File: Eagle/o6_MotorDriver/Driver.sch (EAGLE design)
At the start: 17 parts, among them IC1 ULN2003AD, IC2 REG1117, P1C2 10uF, P1C3 10uF

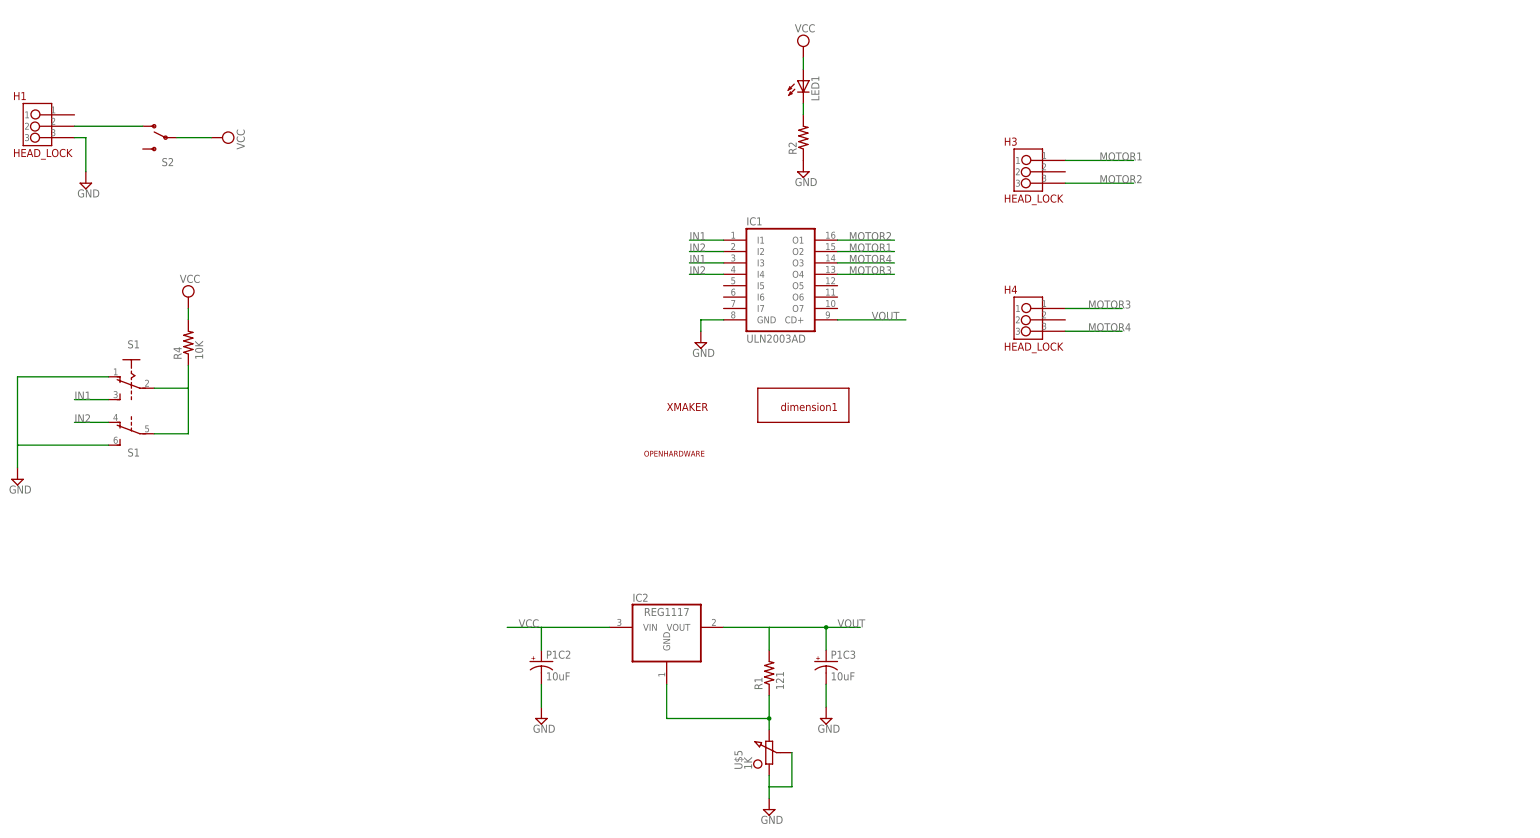
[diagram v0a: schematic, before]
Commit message: change motordriver
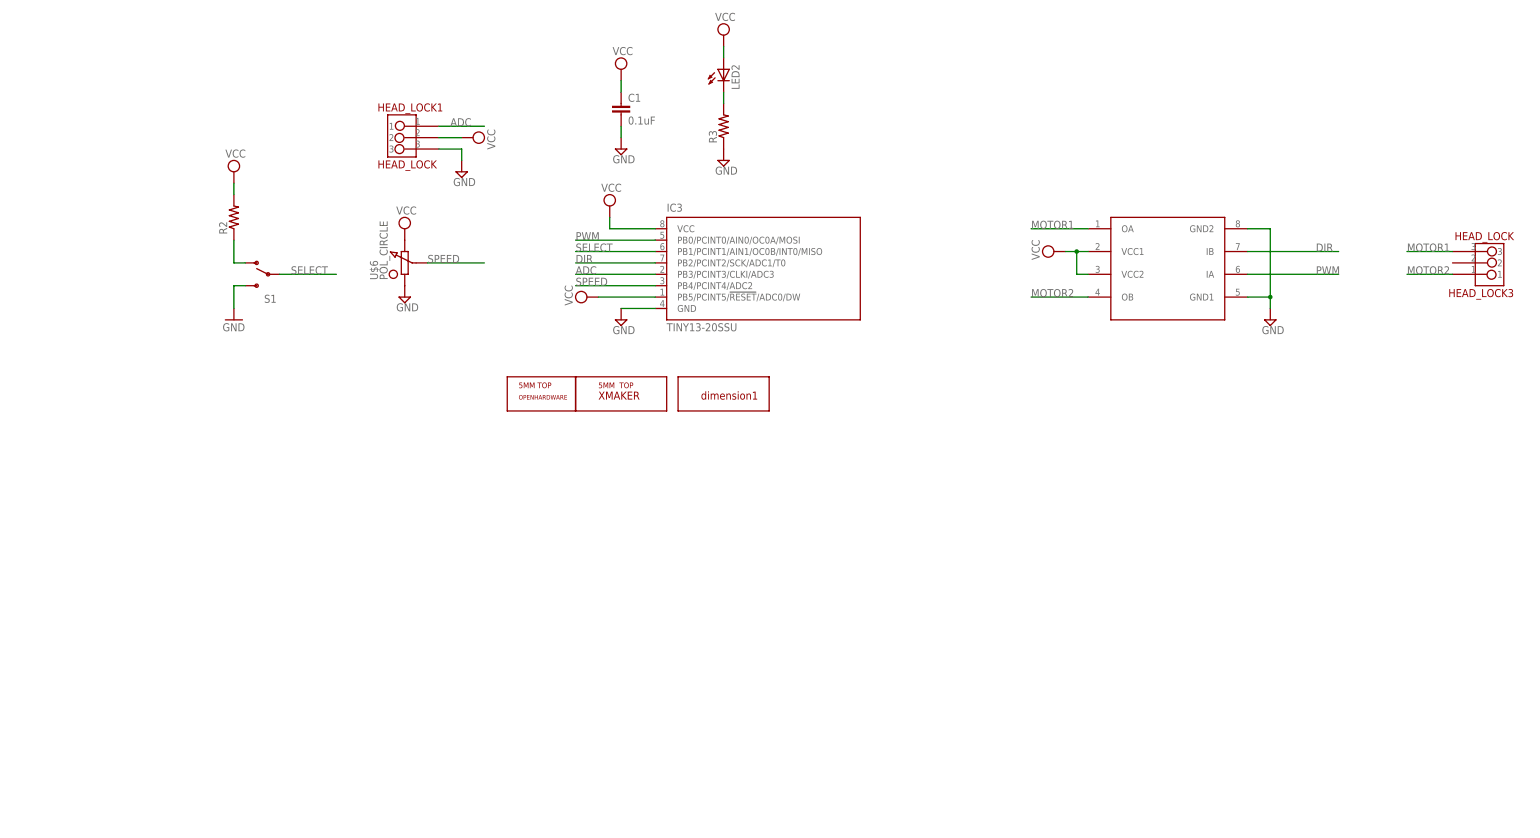
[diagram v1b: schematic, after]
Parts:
- removed H1, H3, H4: HEAD_LOCK, HEAD_LOCK:HEAD_LOCK
- removed IC1: ULN2003AD, uln-udn:ULN2003AD
- removed IC2: REG1117, burr-brown:REG1117
- removed LED1: (no value), eagle-ltspice:LED_ESML0603
- removed P1C2, P1C3: 10uF, SparkFun:CAP_POL1206
- removed R1: 121, SparkFun-Resistors:0.27OHM-1/10W-1%(0603)
- removed R4: 10K, SparkFun-Resistors:0.27OHM-1/10W-1%(0603)
- removed S2: (no value), SparkFun-Electromechanical:SWITCH-SPDTKIT
- removed U$3: DIMENSION1, Xmaker_yuhui:DIMENSION1
- removed U$4: OPENHARDWARE, Xmaker_yuhui:OPENHARDWARE
- removed U$5: 1K, Xmaker_yuhui:POL_CIRCLE
- added C1: 0.1uF, SparkFun-Passives:CAP0603-CAP
- added HEAD_LOCK1, HEAD_LOCK3: HEAD_LOCK, Xmaker_yuhui:HEAD_LOCK
- added IC3: TINY13-20SSU, atmel:TINY13-20SSU
- added LED2: (no value), eagle-ltspice:LED_ESML0603
- added R3: (no value), SparkFun-Resistors:0.27OHM-1/10W-1%(0603)
- added U$1: DIMENSION1, Xmaker_yuhui:DIMENSION1
- added U$6: POL_CIRCLE, Xmaker_yuhui:POL_CIRCLE
- added U$7: XMAKERLOGO_5MM_TOP, Xmaker_yuhui:XMAKERLOGO_5MM_TOP
- added U$8: OPENHARDWARE_5MM_TOP, Xmaker_yuhui:OPENHARDWARE_5MM_TOP
- R2: device SparkFun-Resistors:0.27OHM-1/10W-1%(0603) -> SparkFun-Passives:RESISTOR0603-RES
- S1: device switch:A68-A31 -> SparkFun-Electromechanical:SWITCH-SPDTKIT
- U$2: value XMAKERLOGO2 -> L9110; device Xmaker_yuhui:XMAKERLOGO2 -> Xmaker_yuhui:L9110
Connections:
- removed net IN1: IC1.I1, IC1.I3, S1A.S
- removed net IN2: IC1.I2, IC1.I4, S1B.O
- removed net MOTOR3: H4.1, IC1.O4
- removed net MOTOR4: H4.3, IC1.O3
- removed net N$1: LED1.C, R2.2
- removed net N$3: IC2.GND, R1.1, U$5.1
- removed net N$4: H1.2, S2.O
- removed net VOUT: IC1.CD+, IC2.VOUT, P1C3.+, R1.2
- new net ADC: HEAD_LOCK1.1, IC3.PB3/PCINT3/CLKI/ADC3
- new net DIR: IC3.PB2/PCINT2/SCK/ADC1/T0, U$2.IB
- new net N$5: LED2.C, R3.2
- new net PWM: IC3.PB0/PCINT0/AIN0/OC0A/MOSI, U$2.IA
- new net SELECT: IC3.PB1/PCINT1/AIN1/OC0B/INT0/MISO, S1.P
- new net SPEED: IC3.PB4/PCINT4/ADC2, U$6.2
- net GND: now also C1.2, HEAD_LOCK1.3, IC3.GND, R3.1, S1.S, U$2.GND1, U$2.GND2, U$6.3; no longer H1.3, IC1.GND, P1C2.-, P1C3.-, R2.1, S1A.O, S1B.S, U$5.2, U$5.3
- net MOTOR1: now also HEAD_LOCK3.3, U$2.OA; no longer H3.1, IC1.O2
- net MOTOR2: now also HEAD_LOCK3.1, U$2.OB; no longer H3.3, IC1.O1
- net N$2: now also R2.1, S1.O; no longer R4.1, S1A.P, S1B.P
- net VCC: now also C1.1, HEAD_LOCK1.2, IC3.PB5/PCINT5/!RESET!/ADC0/DW, IC3.VCC, LED2.A, R2.2, U$2.VCC1, U$2.VCC2, U$6.1; no longer IC2.VIN, LED1.A, P1C2.+, R4.2, S2.P
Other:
- moved on the sheet: R2

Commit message: 12.15
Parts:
- removed HEAD_LOCK1, HEAD_LOCK3: HEAD_LOCK, Xmaker_yuhui:HEAD_LOCK
- added HEAD_LOCK2: HEAD_LOCK, Xmaker:HEAD_LOCK
- added U$4: HEAD_LOCK2, Xmaker:HEAD_LOCK2
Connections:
- net ADC: now also HEAD_LOCK2.1; no longer HEAD_LOCK1.1
- net GND: now also HEAD_LOCK2.3; no longer HEAD_LOCK1.3
- net MOTOR1: now also U$4.2; no longer HEAD_LOCK3.3
- net MOTOR2: now also U$4.1; no longer HEAD_LOCK3.1
- net VCC: now also HEAD_LOCK2.2; no longer HEAD_LOCK1.2
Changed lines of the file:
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@@
 <?xml version="1.0" encoding="utf-8"?>
 <!DOCTYPE eagle SYSTEM "eagle.dtd">
-<eagle version="7.2.0">
+<eagle version="6.6.0">
 <drawing>
 <settings>
@@
 <setting verticaltext="up"/>
 </settings>
-<grid distance="0.1" unitdist="inch" unit="inch" style="lines" multiple="1" display="no" altdistance="0.01" altunitdist="inch" altunit="inch"/>
+<grid distance="10" unitdist="mil" unit="mil" style="lines" multiple="1" display="no" altdistance="0.01" altunitdist="inch" altunit="inch"/>
 <layers>
 <layer number="1" name="Top" color="4" fill="1" visible="no" active="no"/>
@@
 <part name="U$1" library="Xmaker_yuhui" deviceset="DIMENSION1" device=""/>
 <part name="U$6" library="Xmaker_yuhui" deviceset="POL_CIRCLE" device=""/>
-<part name="HEAD_LOCK1" library="Xmaker_yuhui" deviceset="HEAD_LOCK" device=""/>
 <part name="U$7" library="Xmaker_yuhui" deviceset="XMAKERLOGO_5MM_TOP" device=""/>
 <part name="U$8" library="Xmaker_yuhui" deviceset="OPENHARDWARE_5MM_TOP" device=""/>
@@
 <part name="SUPPLY1" library="supply2" deviceset="VCC" device=""/>
 <part name="SUPPLY3" library="supply2" deviceset="GND" device=""/>
-<part name="HEAD_LOCK3" library="Xmaker_yuhui" deviceset="HEAD_LOCK" device=""/>
 <part name="SUPPLY2" library="supply2" deviceset="VCC" device=""/>
+<part name="HEAD_LOCK2" library="Xmaker" deviceset="HEAD_LOCK" device=""/>
+<part name="U$4" library="Xmaker" deviceset="HEAD_LOCK2" device=""/>
 </parts>
 <sheets>
@@
 <instance part="U$1" gate="G$1" x="-5.08" y="-25.4"/>
 <instance part="U$6" gate="G$1" x="-76.2" y="5.08"/>
-<instance part="HEAD_LOCK1" gate="G$1" x="-76.2" y="33.02"/>
 <instance part="U$7" gate="G$1" x="-27.94" y="-22.86"/>
 <instance part="U$8" gate="G$1" x="-45.72" y="-25.4"/>
@@
 <instance part="SUPPLY1" gate="G$1" x="68.58" y="7.62" rot="R90"/>
 <instance part="SUPPLY3" gate="GND" x="116.84" y="-7.62"/>
-<instance part="HEAD_LOCK3" gate="G$1" x="165.1" y="5.08" rot="R180"/>
 <instance part="SUPPLY2" gate="G$1" x="-114.3" y="25.4"/>
+<instance part="HEAD_LOCK2" gate="G$1" x="-76.454" y="33.02"/>
+<instance part="U$4" gate="G$1" x="169.926" y="5.08" rot="R180"/>
 </instances>
 <busses>
@@
 <segment>
 <pinref part="SUPPLY9" gate="GND" pin="GND"/>
-<wire x1="-68.58" y1="30.48" x2="-63.5" y2="30.48" width="0.1524" layer="91"/>
+<wire x1="-68.834" y1="30.48" x2="-63.5" y2="30.48" width="0.1524" layer="91"/>
 <wire x1="-63.5" y1="30.48" x2="-63.5" y2="27.94" width="0.1524" layer="91"/>
-<pinref part="HEAD_LOCK1" gate="G$1" pin="3"/>
+<pinref part="HEAD_LOCK2" gate="G$1" pin="3"/>
 </segment>
 <segment>
@@
 <segment>
 <pinref part="SUPPLY10" gate="G$1" pin="VCC"/>
-<wire x1="-63.5" y1="33.02" x2="-68.58" y2="33.02" width="0.1524" layer="91"/>
-<pinref part="HEAD_LOCK1" gate="G$1" pin="2"/>
+<wire x1="-63.5" y1="33.02" x2="-68.834" y2="33.02" width="0.1524" layer="91"/>
+<pinref part="HEAD_LOCK2" gate="G$1" pin="2"/>
 </segment>
 <segment>
@@
 </segment>
 <segment>
-<wire x1="-68.58" y1="35.56" x2="-58.42" y2="35.56" width="0.1524" layer="91"/>
+<wire x1="-68.834" y1="35.56" x2="-58.42" y2="35.56" width="0.1524" layer="91"/>
 <label x="-66.04" y="35.56" size="1.778" layer="95"/>
-<pinref part="HEAD_LOCK1" gate="G$1" pin="1"/>
+<pinref part="HEAD_LOCK2" gate="G$1" pin="1"/>
 </segment>
 </net>
@@
 </segment>
 <segment>
-<pinref part="HEAD_LOCK3" gate="G$1" pin="3"/>
-<wire x1="157.48" y1="7.62" x2="147.32" y2="7.62" width="0.1524" layer="91"/>
-<label x="147.32" y="7.62" size="1.778" layer="95"/>
+<wire x1="159.004" y1="6.35" x2="161.29" y2="6.35" width="0.1524" layer="91"/>
+<wire x1="161.29" y1="6.35" x2="147.828" y2="6.35" width="0.1524" layer="91"/>
+<wire x1="147.828" y1="6.35" x2="147.828" y2="6.604" width="0.1524" layer="91"/>
+<label x="148.336" y="6.35" size="1.778" layer="95"/>
+<pinref part="U$4" gate="G$1" pin="2"/>
+<junction x="161.29" y="6.35"/>
 </segment>
 </net>
@@
 </segment>
 <segment>
-<pinref part="HEAD_LOCK3" gate="G$1" pin="1"/>
-<wire x1="157.48" y1="2.54" x2="147.32" y2="2.54" width="0.1524" layer="91"/>
-<label x="147.32" y="2.54" size="1.778" layer="95"/>
-</segment>
-</net>
+<wire x1="159.004" y1="3.81" x2="161.29" y2="3.81" width="0.1524" layer="91"/>
+<label x="148.082" y="3.556" size="1.778" layer="95"/>
+<pinref part="U$4" gate="G$1" pin="1"/>
+<wire x1="161.29" y1="3.81" x2="148.082" y2="3.81" width="0.1524" layer="91"/>
+<junction x="161.29" y="3.81"/>
+</segment>
+</net>
